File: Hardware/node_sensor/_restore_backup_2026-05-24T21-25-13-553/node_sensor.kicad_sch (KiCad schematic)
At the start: 14 parts, among them J1 Conn_Jack-DC, J2 Pump, J3 Light, U1 DevKitESP32, U2 DHT11, U3 BH1750, U4 ADS1115, U5 DS3231, U6 Soil-Moisture, U7 Soil-Moisture, U8 Soil-Moisture, U9 Soil-Moisture

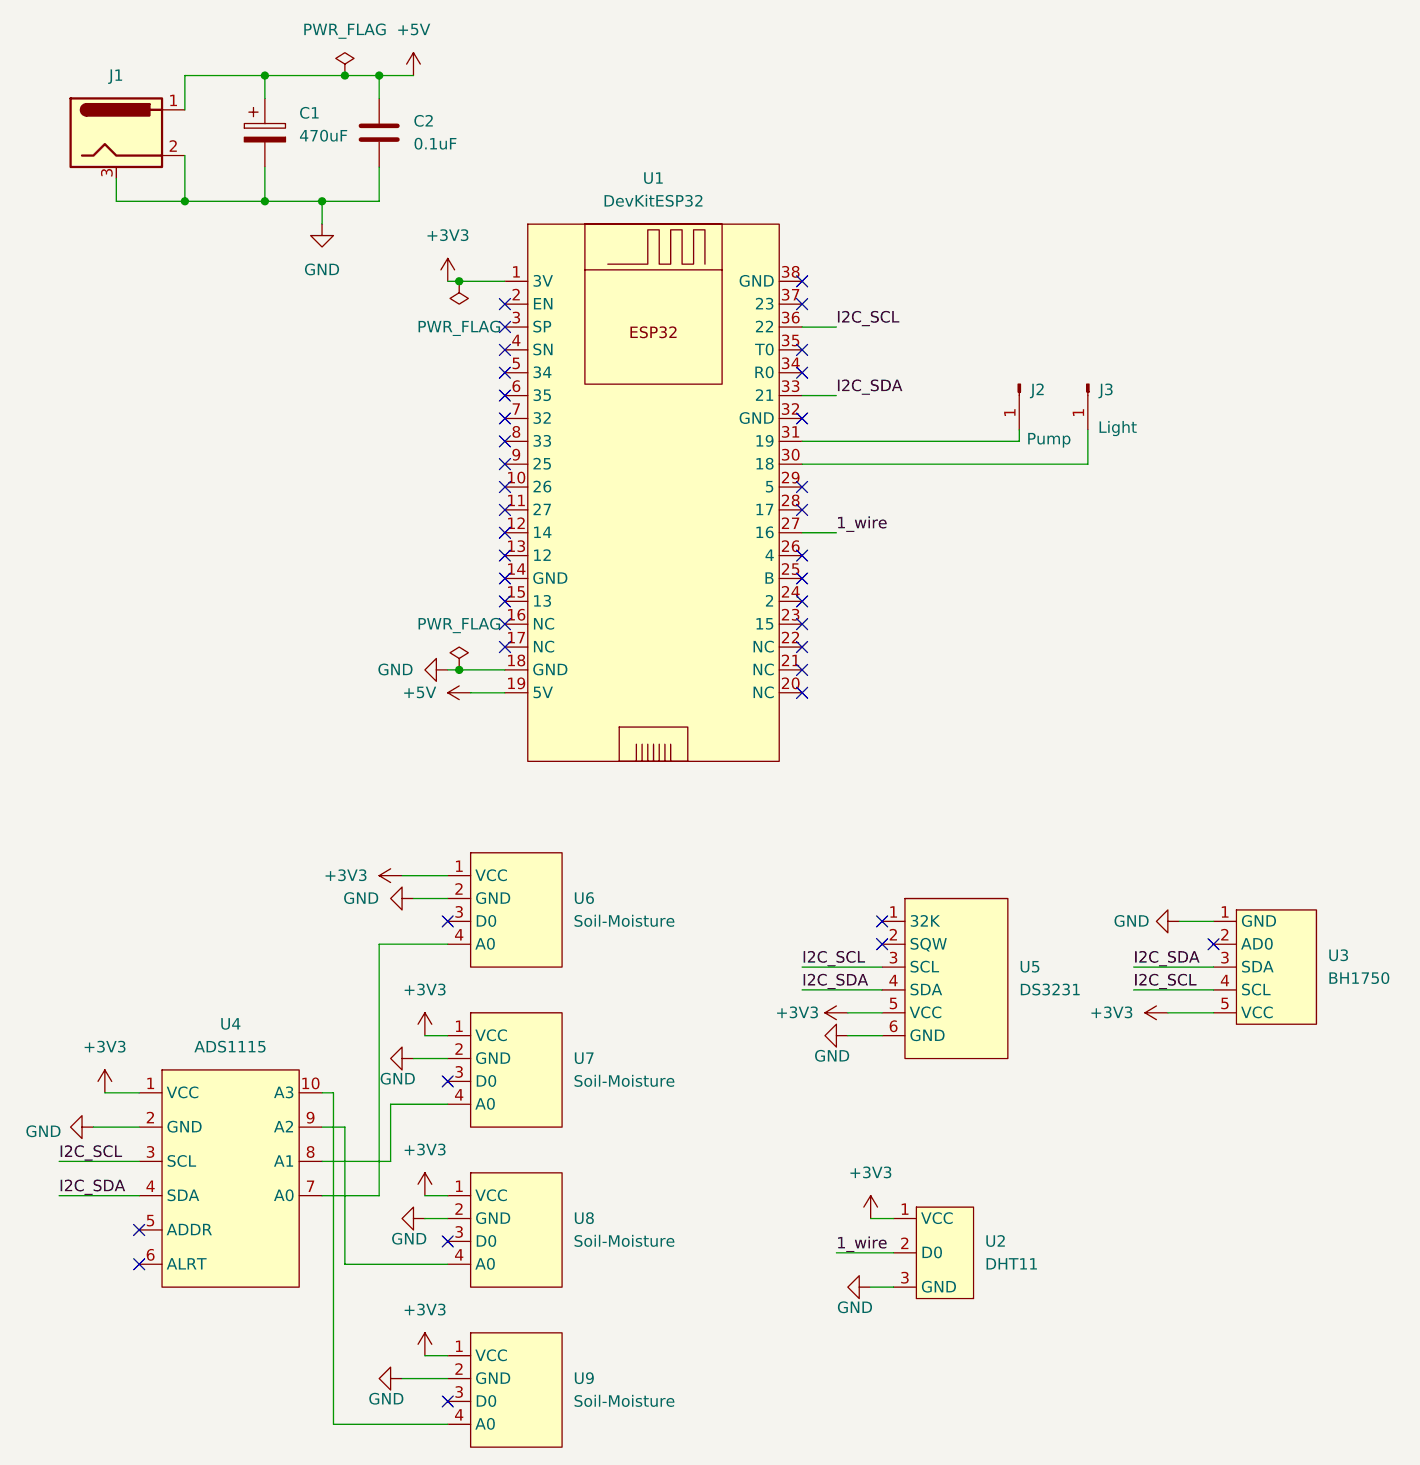
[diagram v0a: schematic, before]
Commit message: updated hardware + fixed conflict Gatway
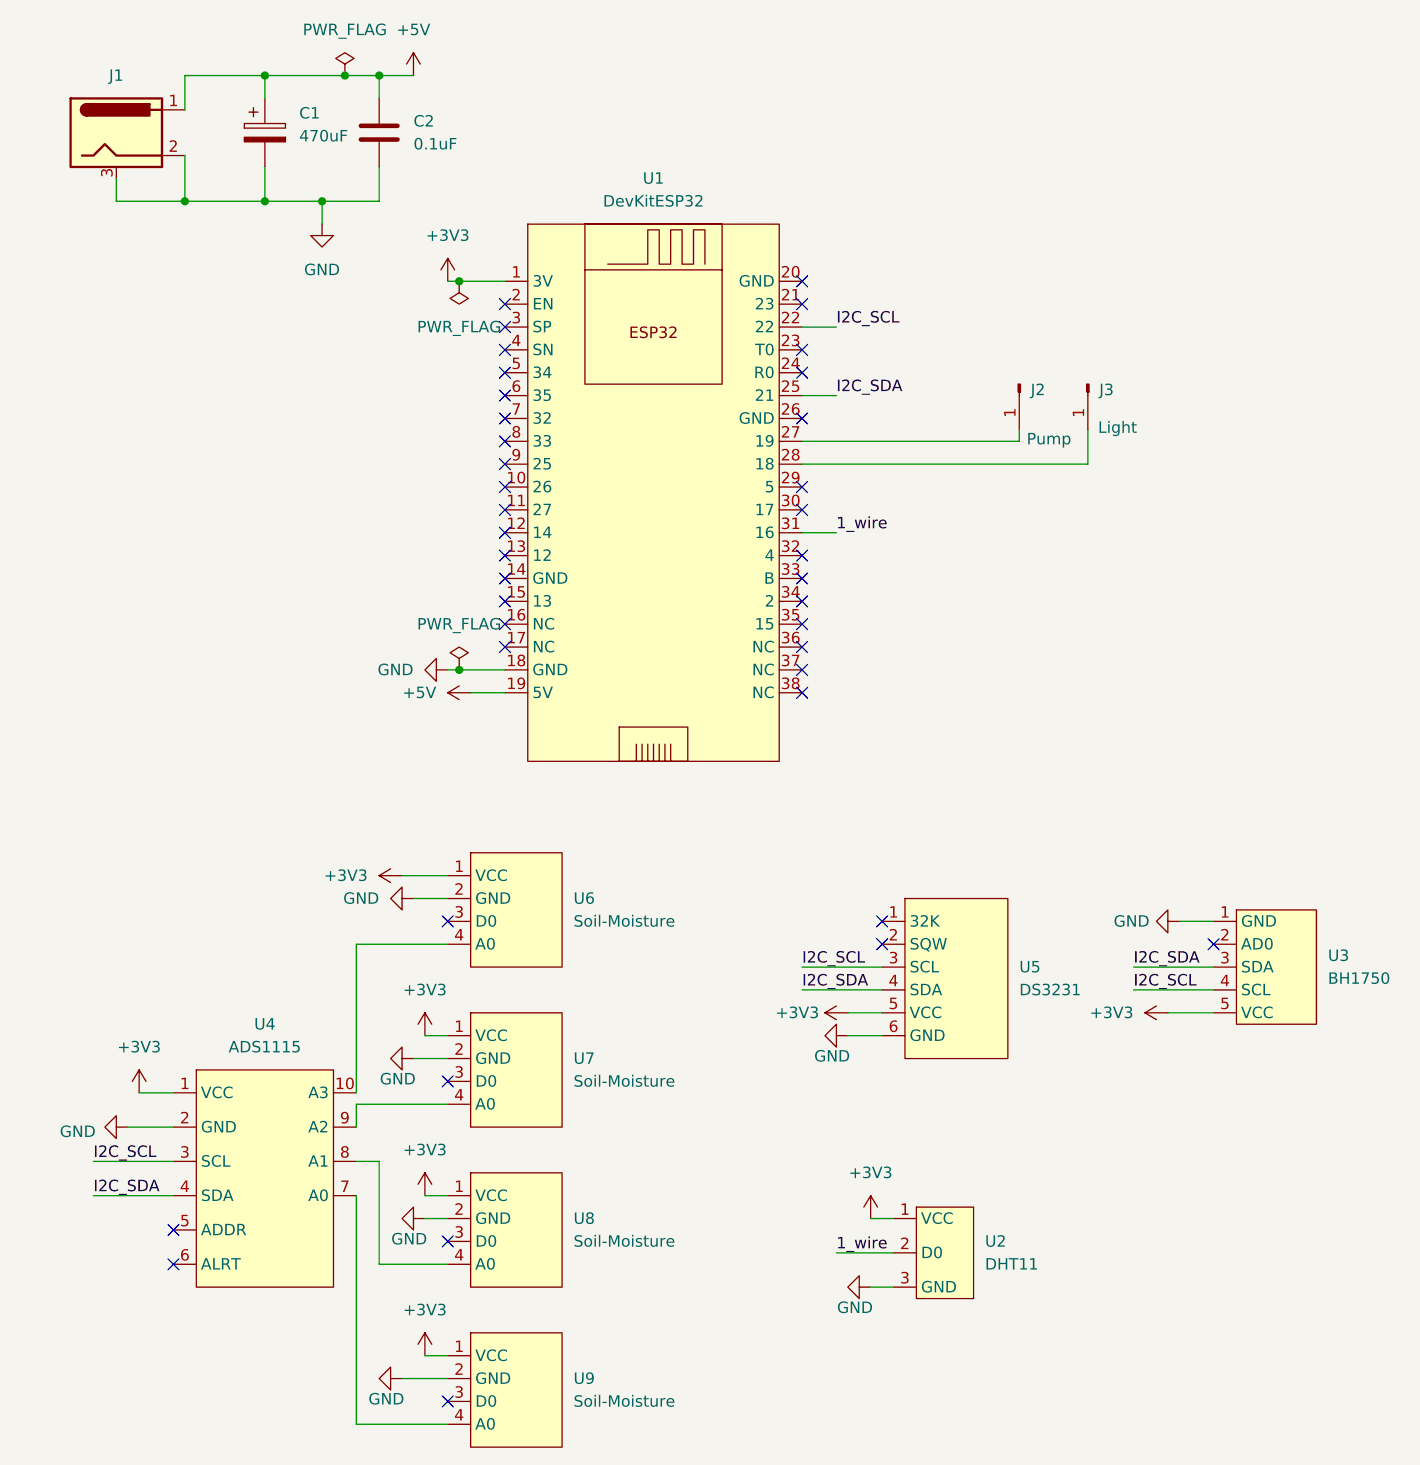
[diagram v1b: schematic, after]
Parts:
- C1: footprint MY_FOOTPRINTS:CP_Elec_6.3x7.7 -> MY_FOOTPRINTS:CP_Elec_10x10.5
- J1: footprint MY_FOOTPRINTS:BarrelJack_Horizontal -> MY_FOOTPRINTS:BarrelJackDC_CLIFF_FC681465S_SMT_Horizontal
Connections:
- net 1_wire: now also U1.31 (16); no longer U1.27 (16)
- net I2C_SCL: now also U1.22; no longer U1.36 (22)
- net I2C_SDA: now also U1.25 (21); no longer U1.33 (21)
- net at U4.10 (A3): now also U6.4 (A0); no longer U9.4 (A0)
- net at U4.7 (A0): now also U9.4 (A0); no longer U6.4 (A0)
- net at U4.8 (A1): now also U8.4 (A0); no longer U7.4 (A0)
- net at U4.9 (A2): now also U7.4 (A0); no longer U8.4 (A0)
- net at U1.28 (18): now also J3.1 (Pin_1)
- net at U1.30 (17): no longer J3.1 (Pin_1)
- net at J2.1 (Pin_1): now also U1.27 (19); no longer U1.31 (19)
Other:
- moved on the sheet: U4
